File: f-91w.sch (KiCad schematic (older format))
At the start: 40 parts, among them P10 CONN_01X01, P11 CONN_01X01, P13 CONN_01X01, P14 CONN_01X01, P5 CONN_01X01, P6 CONN_01X01, P7 CONN_01X01, P8 CONN_01X01, P9 CONN_01X01, Q1 BC846, U1 CY8C4248LQI-BL483, U2 LCD-F-91W, Y1 32.768KHz, Y2 24MHz

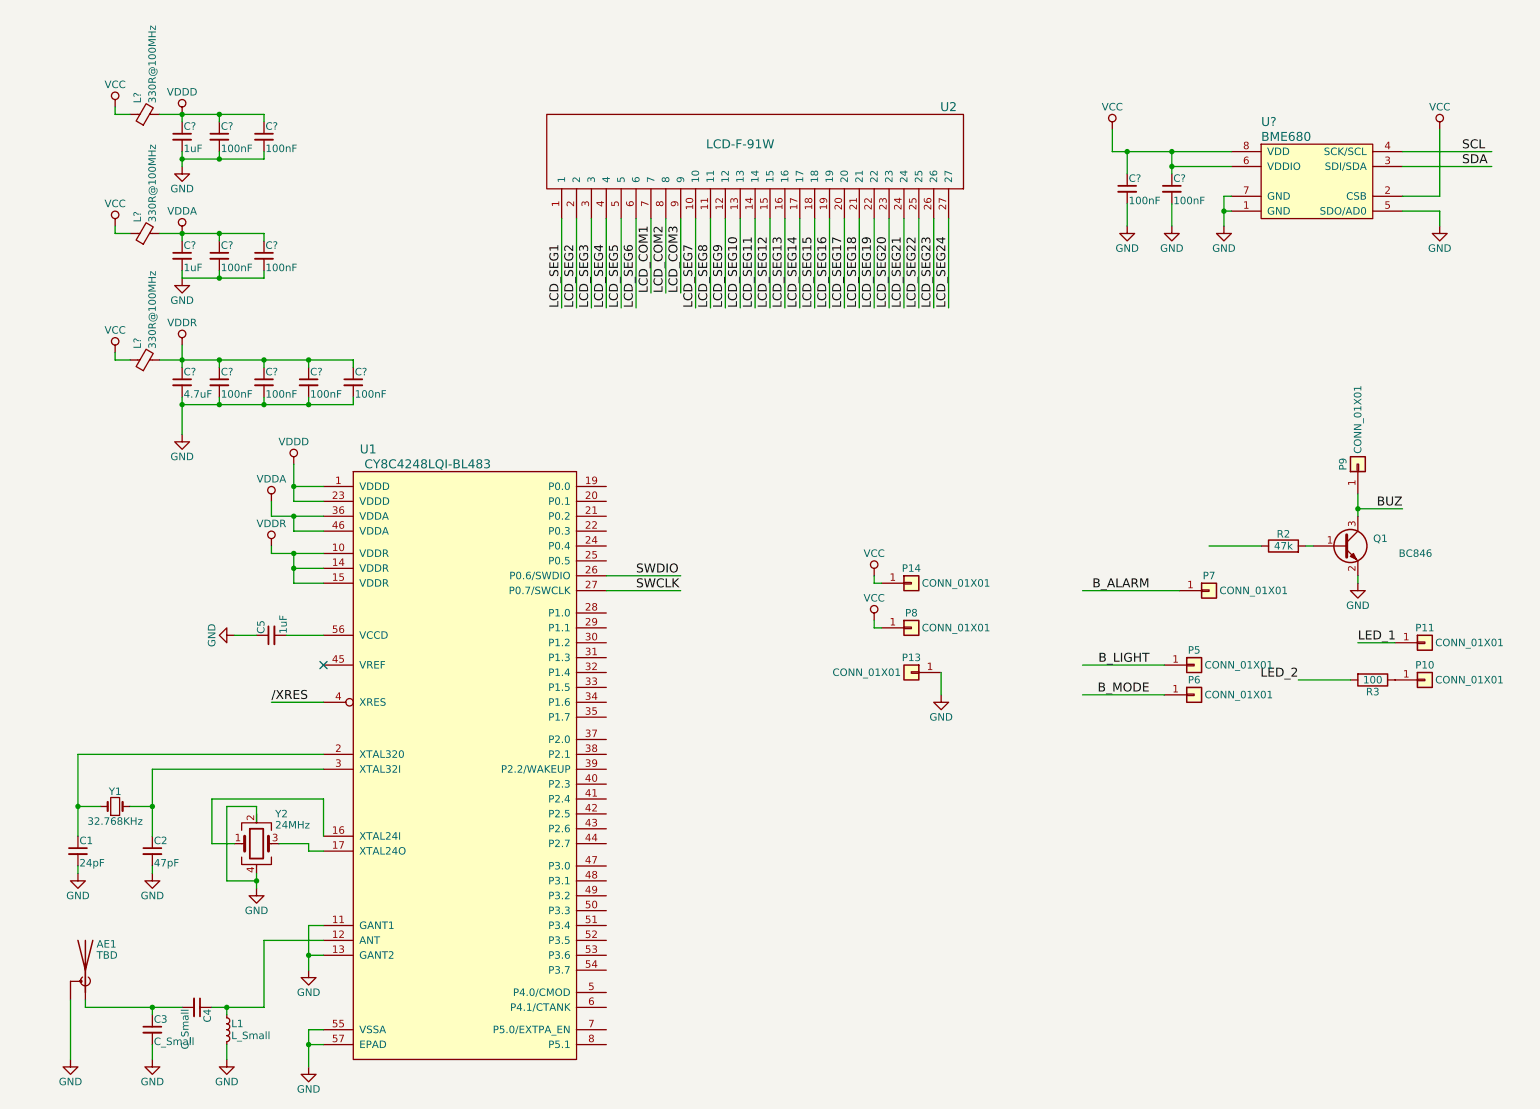
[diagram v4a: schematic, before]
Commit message: Add capacitor footprints
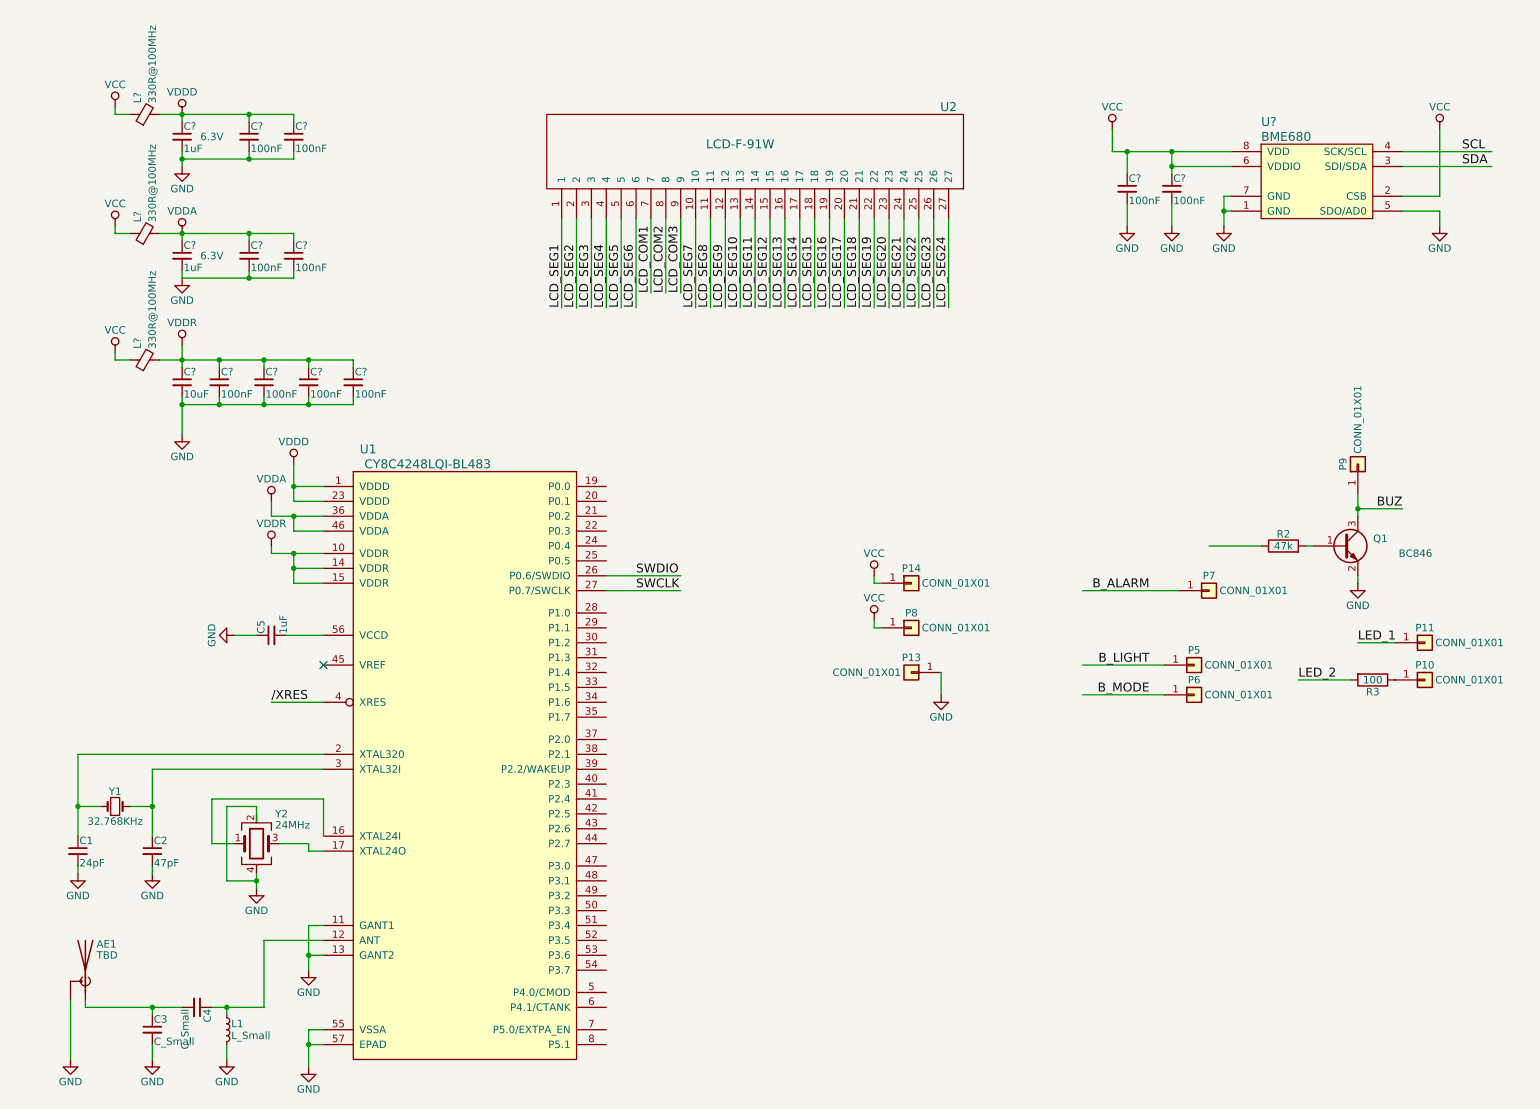
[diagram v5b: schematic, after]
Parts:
- C1, C2, C5, C? (x2): footprint (none) -> Capacitors_SMD:C_0201_NoSilk
- C3, C4: footprint (none) -> Capacitors_SMD:C_0402
- C?: value 4.7uF -> 10uF; MPN (none) -> GRJ155R60J106ME11; Tolerance (none) -> 15%; Voltage (none) -> 6.3V
- C? (x2): Voltage (none) -> 6.3V
- L1: footprint (none) -> Resistors_SMD:R_0402
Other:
- moved on the sheet: C?
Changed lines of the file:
@@
 Text Label 8400 5050 2    60   ~ 0
 B_MODE
-Text Label 9400 4950 2    60   ~ 0
+Text Label 9400 4950 0    60   ~ 0
 LED_2
 $Comp
@@
 F 0 "C1" H 1210 6170 50  0000 L CNN
 F 1 "24pF" H 1210 6020 50  0000 L CNN
-F 2 "" H 1200 6100 50  0001 C CNN
+F 2 "Capacitors_SMD:C_0201_NoSilk" H 1200 6100 50  0001 C CNN
 F 3 "" H 1200 6100 50  0001 C CNN
 	1    1200 6100
@@
 F 0 "C2" H 1710 6170 50  0000 L CNN
 F 1 "47pF" H 1710 6020 50  0000 L CNN
-F 2 "" H 1700 6100 50  0001 C CNN
+F 2 "Capacitors_SMD:C_0201_NoSilk" H 1700 6100 50  0001 C CNN
 F 3 "" H 1700 6100 50  0001 C CNN
 	1    1700 6100
@@
 F 0 "L1" H 2230 7340 50  0000 L CNN
 F 1 "L_Small" H 2230 7260 50  0000 L CNN
-F 2 "" H 2200 7300 50  0001 C CNN
+F 2 "Resistors_SMD:R_0402" H 2200 7300 50  0001 C CNN
 F 3 "" H 2200 7300 50  0001 C CNN
 	1    2200 7300
@@
 F 0 "C4" H 2010 7220 50  0000 L CNN
 F 1 "C_Small" H 2010 7070 50  0000 L CNN
-F 2 "" H 2000 7150 50  0001 C CNN
+F 2 "Capacitors_SMD:C_0402" H 2000 7150 50  0001 C CNN
 F 3 "" H 2000 7150 50  0001 C CNN
 	1    2000 7150
@@
 F 0 "C3" H 1710 7370 50  0000 L CNN
 F 1 "C_Small" H 1710 7220 50  0000 L CNN
-F 2 "" H 1700 7300 50  0001 C CNN
+F 2 "Capacitors_SMD:C_0402" H 1700 7300 50  0001 C CNN
 F 3 "" H 1700 7300 50  0001 C CNN
 	1    1700 7300
@@
 F 0 "C5" H 2510 4720 50  0000 L CNN
 F 1 "1uF" H 2510 4570 50  0000 L CNN
-F 2 "" H 2500 4650 50  0001 C CNN
+F 2 "Capacitors_SMD:C_0201_NoSilk" H 2500 4650 50  0001 C CNN
 F 3 "" H 2500 4650 50  0001 C CNN
 	1    2500 4650
@@
 F 0 "C?" H 8560 1720 50  0000 L CNN
 F 1 "100nF" H 8560 1570 50  0000 L CNN
-F 2 "" H 8550 1650 50  0001 C CNN
+F 2 "Capacitors_SMD:C_0201_NoSilk" H 8550 1650 50  0001 C CNN
 F 3 "" H 8550 1650 50  0001 C CNN
 	1    8550 1650
@@
 F 0 "C?" H 8260 1720 50  0000 L CNN
 F 1 "100nF" H 8260 1570 50  0000 L CNN
-F 2 "" H 8250 1650 50  0001 C CNN
+F 2 "Capacitors_SMD:C_0201_NoSilk" H 8250 1650 50  0001 C CNN
 F 3 "" H 8250 1650 50  0001 C CNN
 	1    8250 1650
@@
 P 1900 2950
 F 0 "C?" H 1910 3020 50  0000 L CNN
-F 1 "4.7uF" H 1910 2870 50  0000 L CNN
+F 1 "10uF" H 1910 2870 50  0000 L CNN
 F 2 "Capacitors_SMD:C_0402" H 1900 2950 50  0001 C CNN
 F 3 "" H 1900 2950 50  0001 C CNN
+F 4 "GRJ155R60J106ME11" H 1900 2950 60  0001 C CNN "MPN"
+F 5 "6.3V" H 1900 2950 60  0001 C CNN "Voltage"
+F 6 "15%" H 1900 2950 60  0001 C CNN "Tolerance"
 	1    1900 2950
 	1    0    0    -1
@@
 F 2 "Capacitors_SMD:C_0201_NoSilk" H 1900 2100 50  0001 C CNN
 F 3 "" H 1900 2100 50  0001 C CNN
+F 4 "6.3V" H 2100 2100 50  0000 C CNN "Voltage"
 	1    1900 2100
 	1    0    0    -1
@@
 F 2 "Capacitors_SMD:C_0201_NoSilk" H 1900 1300 50  0001 C CNN
 F 3 "" H 1900 1300 50  0001 C CNN
+F 4 "6.3V" H 2100 1300 50  0000 C CNN "Voltage"
 	1    1900 1300
 	1    0    0    -1
@@
 L C_Small C?
 U 1 1 5A6DE39C
-P 2150 2100
-F 0 "C?" H 2160 2170 50  0000 L CNN
-F 1 "100nF" H 2160 2020 50  0000 L CNN
-F 2 "Capacitors_SMD:C_0201_NoSilk" H 2150 2100 50  0001 C CNN
-F 3 "" H 2150 2100 50  0001 C CNN
-	1    2150 2100
+P 2350 2100
+F 0 "C?" H 2360 2170 50  0000 L CNN
+F 1 "100nF" H 2360 2020 50  0000 L CNN
+F 2 "Capacitors_SMD:C_0201_NoSilk" H 2350 2100 50  0001 C CNN
+F 3 "" H 2350 2100 50  0001 C CNN
+	1    2350 2100
 	1    0    0    -1
 $EndComp
@@
 L C_Small C?
 U 1 1 5A6DE432
-P 2450 2100
-F 0 "C?" H 2460 2170 50  0000 L CNN
-F 1 "100nF" H 2460 2020 50  0000 L CNN
-F 2 "Capacitors_SMD:C_0201_NoSilk" H 2450 2100 50  0001 C CNN
-F 3 "" H 2450 2100 50  0001 C CNN
-	1    2450 2100
+P 2650 2100
+F 0 "C?" H 2660 2170 50  0000 L CNN
+F 1 "100nF" H 2660 2020 50  0000 L CNN
+F 2 "Capacitors_SMD:C_0201_NoSilk" H 2650 2100 50  0001 C CNN
+F 3 "" H 2650 2100 50  0001 C CNN
+	1    2650 2100
 	1    0    0    -1
 $EndComp
@@
 L C_Small C?
 U 1 1 5A6DE4CB
-P 2150 1300
-F 0 "C?" H 2160 1370 50  0000 L CNN
-F 1 "100nF" H 2160 1220 50  0000 L CNN
-F 2 "Capacitors_SMD:C_0201_NoSilk" H 2150 1300 50  0001 C CNN
-F 3 "" H 2150 1300 50  0001 C CNN
-	1    2150 1300
+P 2350 1300
+F 0 "C?" H 2360 1370 50  0000 L CNN
+F 1 "100nF" H 2360 1220 50  0000 L CNN
+F 2 "Capacitors_SMD:C_0201_NoSilk" H 2350 1300 50  0001 C CNN
+F 3 "" H 2350 1300 50  0001 C CNN
+	1    2350 1300
 	1    0    0    -1
 $EndComp
@@
 L C_Small C?
 U 1 1 5A6DE56F
-P 2450 1300
-F 0 "C?" H 2460 1370 50  0000 L CNN
-F 1 "100nF" H 2460 1220 50  0000 L CNN
-F 2 "Capacitors_SMD:C_0201_NoSilk" H 2450 1300 50  0001 C CNN
-F 3 "" H 2450 1300 50  0001 C CNN
-	1    2450 1300
+P 2650 1300
+F 0 "C?" H 2660 1370 50  0000 L CNN
+F 1 "100nF" H 2660 1220 50  0000 L CNN
+F 2 "Capacitors_SMD:C_0201_NoSilk" H 2650 1300 50  0001 C CNN
+F 3 "" H 2650 1300 50  0001 C CNN
+	1    2650 1300
 	1    0    0    -1
 $EndComp
@@
 	1900 1400 1900 1500
 Wire Wire Line
-	1750 1150 2450 1150
-Wire Wire Line
-	2150 1150 2150 1200
-Wire Wire Line
-	2450 1150 2450 1200
-Connection ~ 2150 1150
-Wire Wire Line
-	2150 1400 2150 1450
-Wire Wire Line
-	1900 1450 2450 1450
+	1750 1150 2650 1150
+Wire Wire Line
+	2350 1150 2350 1200
+Wire Wire Line
+	2650 1150 2650 1200
+Connection ~ 2350 1150
+Wire Wire Line
+	2350 1400 2350 1450
+Wire Wire Line
+	1900 1450 2650 1450
 Connection ~ 1900 1450
 Wire Wire Line
-	2450 1450 2450 1400
-Connection ~ 2150 1450
+	2650 1450 2650 1400
+Connection ~ 2350 1450
 Wire Wire Line
 	1900 1950 1900 2000
@@
 	1900 2200 1900 2250
 Wire Wire Line
-	1900 2250 2450 2250
-Wire Wire Line
-	2150 2250 2150 2200
-Wire Wire Line
-	2450 2250 2450 2200
-Connection ~ 2150 2250
-Wire Wire Line
-	2150 2000 2150 1950
-Wire Wire Line
-	2450 1950 2450 2000
-Connection ~ 2150 1950
+	1900 2250 2650 2250
+Wire Wire Line
+	2350 2250 2350 2200
+Wire Wire Line
+	2650 2250 2650 2200
+Connection ~ 2350 2250
+Wire Wire Line
+	2350 2000 2350 1950
+Wire Wire Line
+	2650 1950 2650 2000
+Connection ~ 2350 1950
 Connection ~ 1900 1950
 Wire Wire Line
-	1750 1950 2450 1950
+	1750 1950 2650 1950
 Connection ~ 1900 1150
 $Comp

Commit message: Create (unfinished) QFN56 footprint
TODO: Customise paste mask to avoid excess solder on centre pad
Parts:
- U1: footprint (none) -> f-91w:Cypress_QFN56
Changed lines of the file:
@@
 F 0 "U1" H 3150 7400 60  0000 C CNN
 F 1 "CY8C4248LQI-BL483" H 3550 7300 60  0000 C CNN
-F 2 "" H 3750 7400 60  0001 C CNN
+F 2 "f-91w:Cypress_QFN56" H 3750 7400 60  0001 C CNN
 F 3 "" H 3750 7400 60  0001 C CNN
 	1    3800 5400

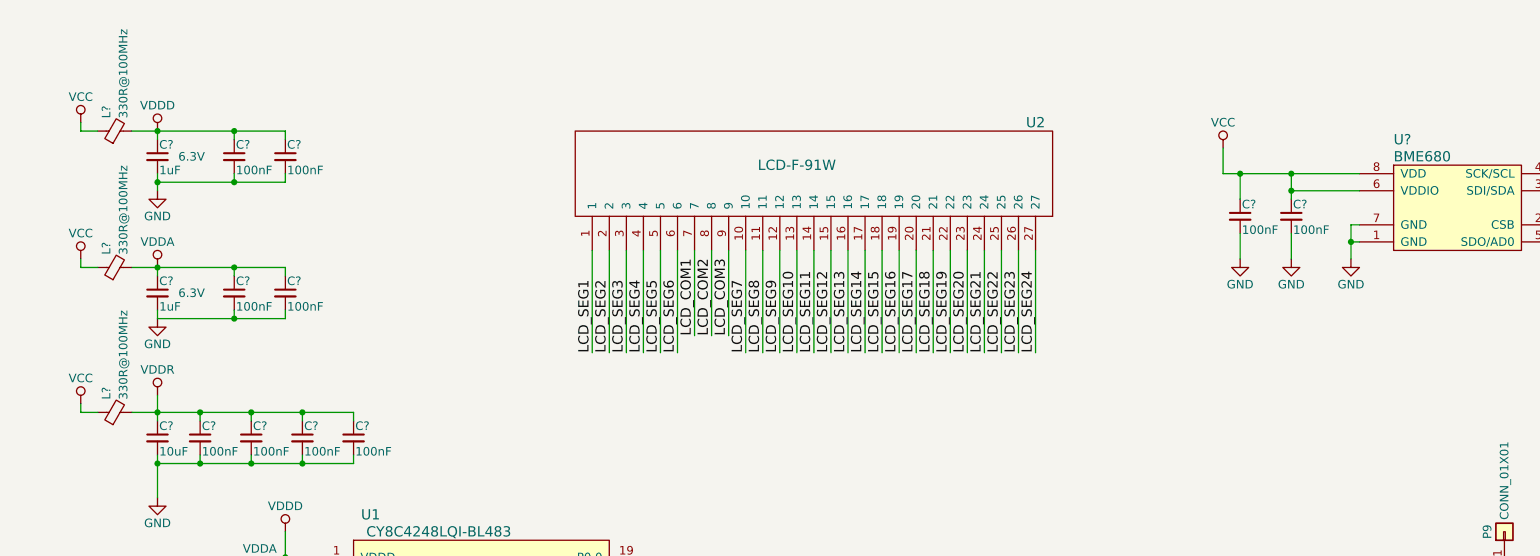
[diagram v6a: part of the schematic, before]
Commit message: PCB: First import to PCB. Lots of changes, move to 4 layer.
Components in roughly right position, all existing traces ripped up.
Lets us see how much space we have for BLE antenna, roughly 6.5x4x1.5mm
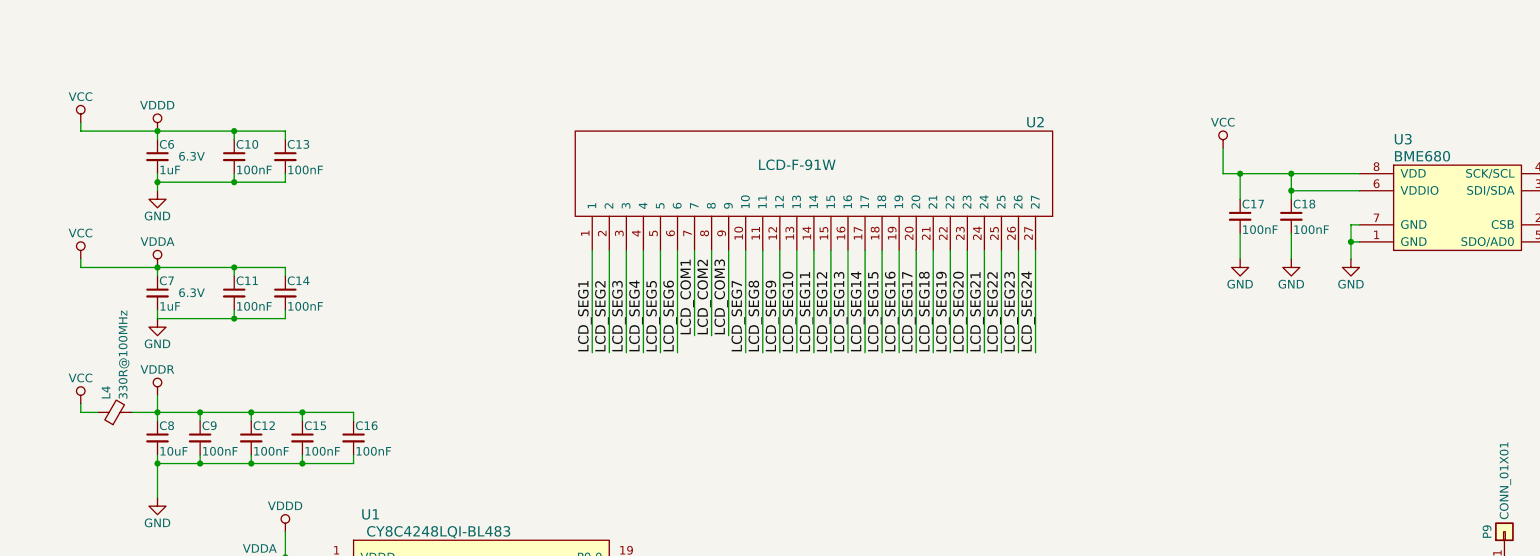
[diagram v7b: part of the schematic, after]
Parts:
- removed L? (x2): 330R@100MHz, Resistors_SMD:R_0201_NoSilk, symbol Ferrite_Bead_Small
- R2: footprint Resistors_SMD:R_0402 -> Resistors_SMD:R_0201_NoSilk
- R3: footprint Resistors_SMD:R_0402 -> Resistors_SMD:R_0201
- U3: renamed from U?; footprint (none) -> f-91w:BME680
- Y1: footprint (none) -> Crystals:Crystal_SMD_TXC_9HT11-2pin_2.0x1.2mm; MPN (none) -> ABS06-32.768KHZ-1-T
- Y2: footprint (none) -> Crystals:Crystal_SMD_2016-4pin_2.0x1.6mm; MPN (none) -> Q22FA12800249
- gave numbers to parts that had none: 14
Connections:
- wire segments 145 -> 143
